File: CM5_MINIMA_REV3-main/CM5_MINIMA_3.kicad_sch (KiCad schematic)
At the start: 20 parts, among them J101 TYPEC-305-ACP16H458, SW101 MK-11C04-G013

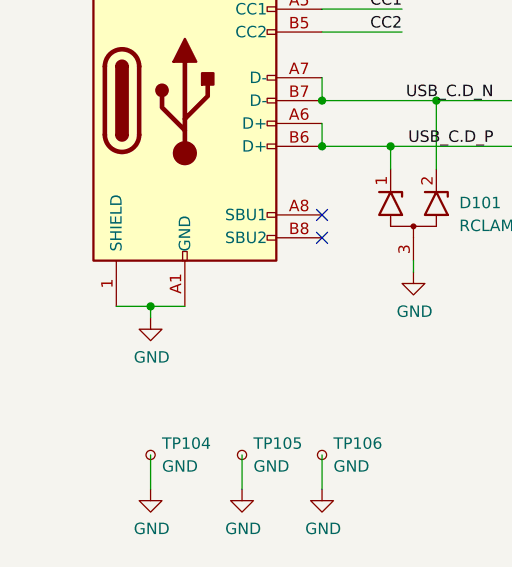
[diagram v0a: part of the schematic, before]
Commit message: warning fix - 17 left
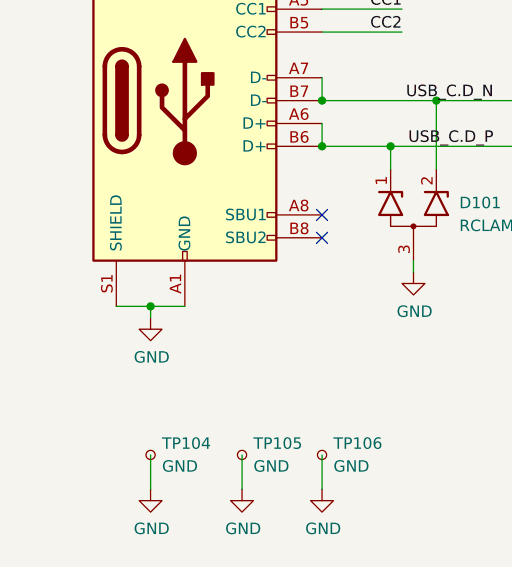
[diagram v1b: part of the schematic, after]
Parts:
- J101: footprint EasyEDA:USB-C-SMD_TYPEC-305-ACP16H458 -> CM5_MINIMA_local:USB-C-SMD_TYPEC-305-ACP16H458
- SW101: footprint EasyEDA:SW-SMD_MK-11C04-G013 -> CM5_MINIMA_local:SW-SMD_MK-11C04-G013
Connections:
- net GND: now also J101.S1 (SHIELD); no longer J101.1 (SHIELD)
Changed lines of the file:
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@@
 			)
 		)
-		(property "Footprint" "EasyEDA:USB-C-SMD_TYPEC-305-ACP16H458"
+		(property "Footprint" "CM5_MINIMA_local:USB-C-SMD_TYPEC-305-ACP16H458"
 			(at 39.37 74.93 0)
 			(effects
@@
 			)
 		)
-		(property "Description" "Connector_USB:USB_C_Receptacle_GCT_USB4105-xx-A_16P_TopMnt_Horizontal"
+		(property "Description" "USB 2.0-only 16P Type-C Receptacle connector"
 			(at 35.56 74.93 0)
 			(effects
@@
 		(pin "B9"
 		)
-		(pin "1"
+		(pin "S1"
 		)
 		(instances
@@
 			)
 		)
-		(property "Footprint" "EasyEDA:SW-SMD_MK-11C04-G013"
+		(property "Footprint" "CM5_MINIMA_local:SW-SMD_MK-11C04-G013"
 			(at 85.09 162.56 0)
 			(effects

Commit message: relay after layout design
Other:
- company: Pierluigi Colangeli -> (none)
- title: CM5 MINIMA -> CM5 MINIMA Modified

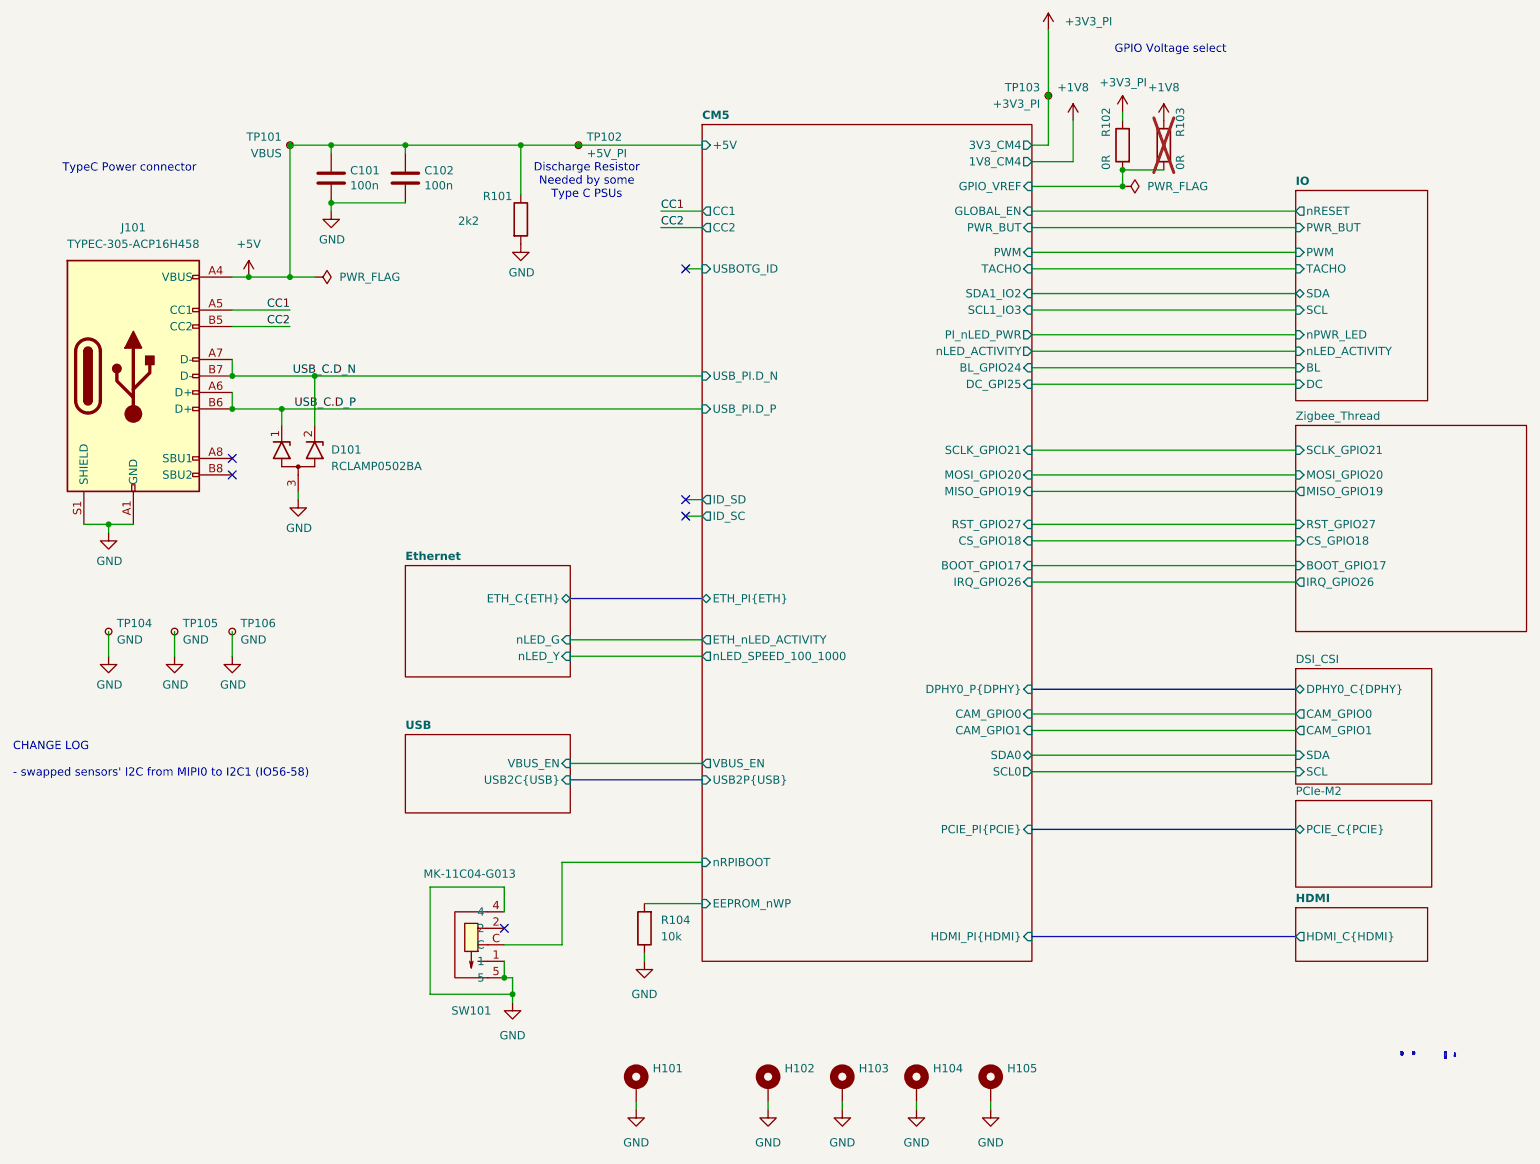
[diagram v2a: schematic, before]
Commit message: Revert CM5_MINIMA_REV3-main to pre-warning-fix state (feae2c2) - fix component mismatches
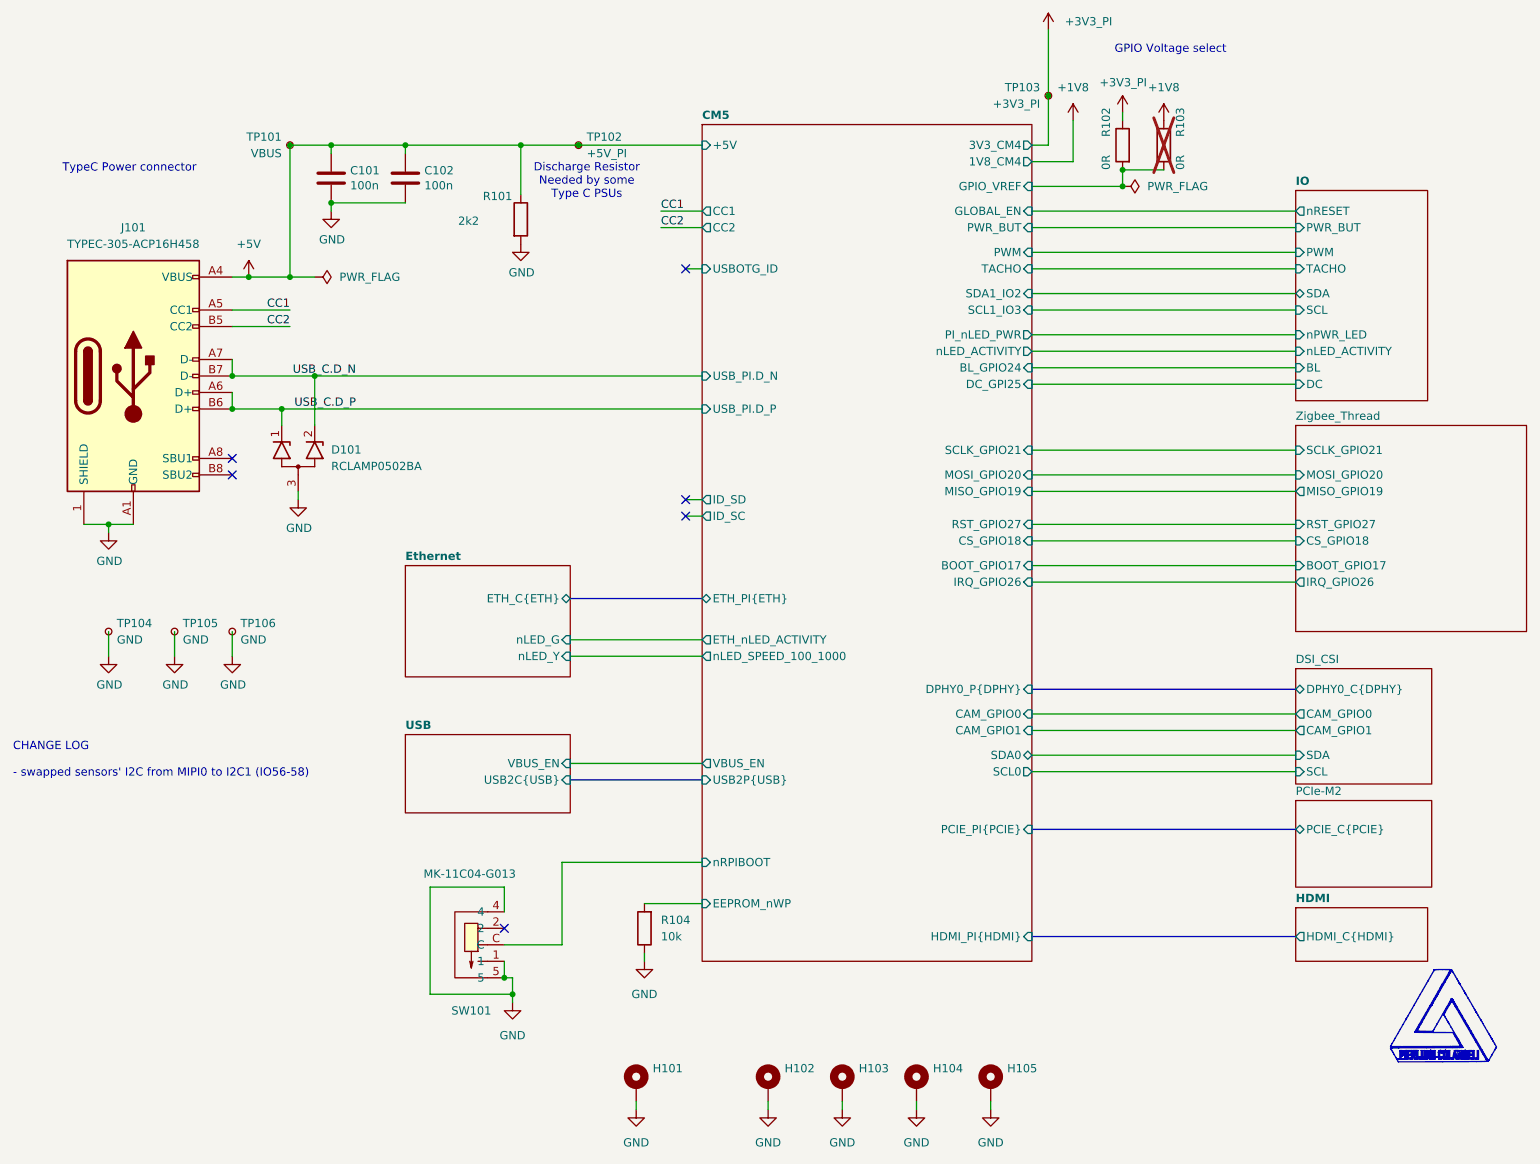
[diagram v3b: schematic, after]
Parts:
- J101: footprint CM5_MINIMA_local:USB-C-SMD_TYPEC-305-ACP16H458 -> EasyEDA:USB-C-SMD_TYPEC-305-ACP16H458
- SW101: footprint CM5_MINIMA_local:SW-SMD_MK-11C04-G013 -> EasyEDA:SW-SMD_MK-11C04-G013
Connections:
- net GND: now also J101.1 (SHIELD); no longer J101.S1 (SHIELD)
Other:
- company: (none) -> Pierluigi Colangeli
- title: CM5 MINIMA Modified -> CM5 MINIMA

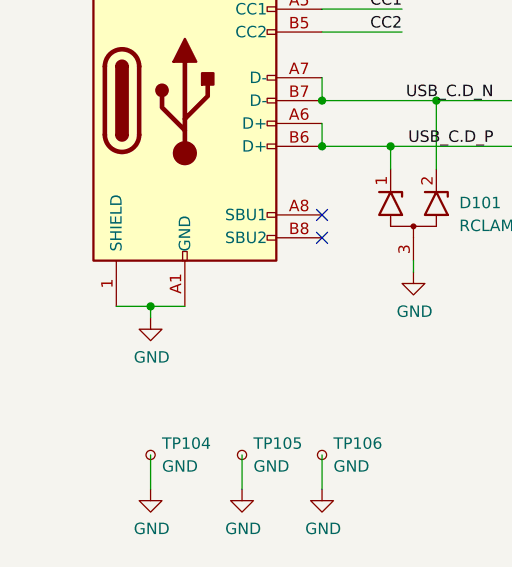
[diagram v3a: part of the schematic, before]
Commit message: with old version retraced and fixing
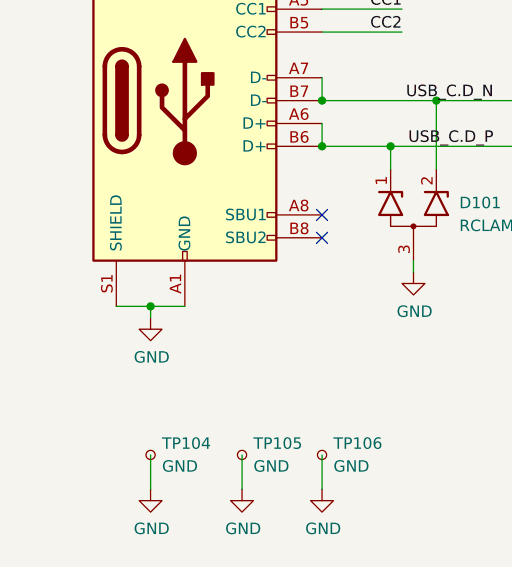
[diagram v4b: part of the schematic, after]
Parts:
- SW101: footprint EasyEDA:SW-SMD_MK-11C04-G013 -> easyeda2kicad:SW-SMD_MK-11C04-G013
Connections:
- net GND: now also J101.S1 (SHIELD); no longer J101.1 (SHIELD)
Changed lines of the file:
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@@
 			)
 		)
-		(property "Description" "Connector_USB:USB_C_Receptacle_GCT_USB4105-xx-A_16P_TopMnt_Horizontal"
+		(property "Description" "USB 2.0-only 16P Type-C Receptacle connector"
 			(at 35.56 74.93 0)
 			(effects
@@
 		(pin "B9"
 		)
-		(pin "1"
+		(pin "S1"
 		)
 		(instances
@@
 			)
 		)
-		(property "Footprint" "EasyEDA:SW-SMD_MK-11C04-G013"
+		(property "Footprint" "easyeda2kicad:SW-SMD_MK-11C04-G013"
 			(at 85.09 162.56 0)
 			(effects
